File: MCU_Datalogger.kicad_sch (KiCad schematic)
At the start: 25 parts, among them U1 24LC1025, U2 24LC1025, U3 DS1337S_, U4 ATMEGA328P-AUR, Y1 Crystal, Y2 Crystal

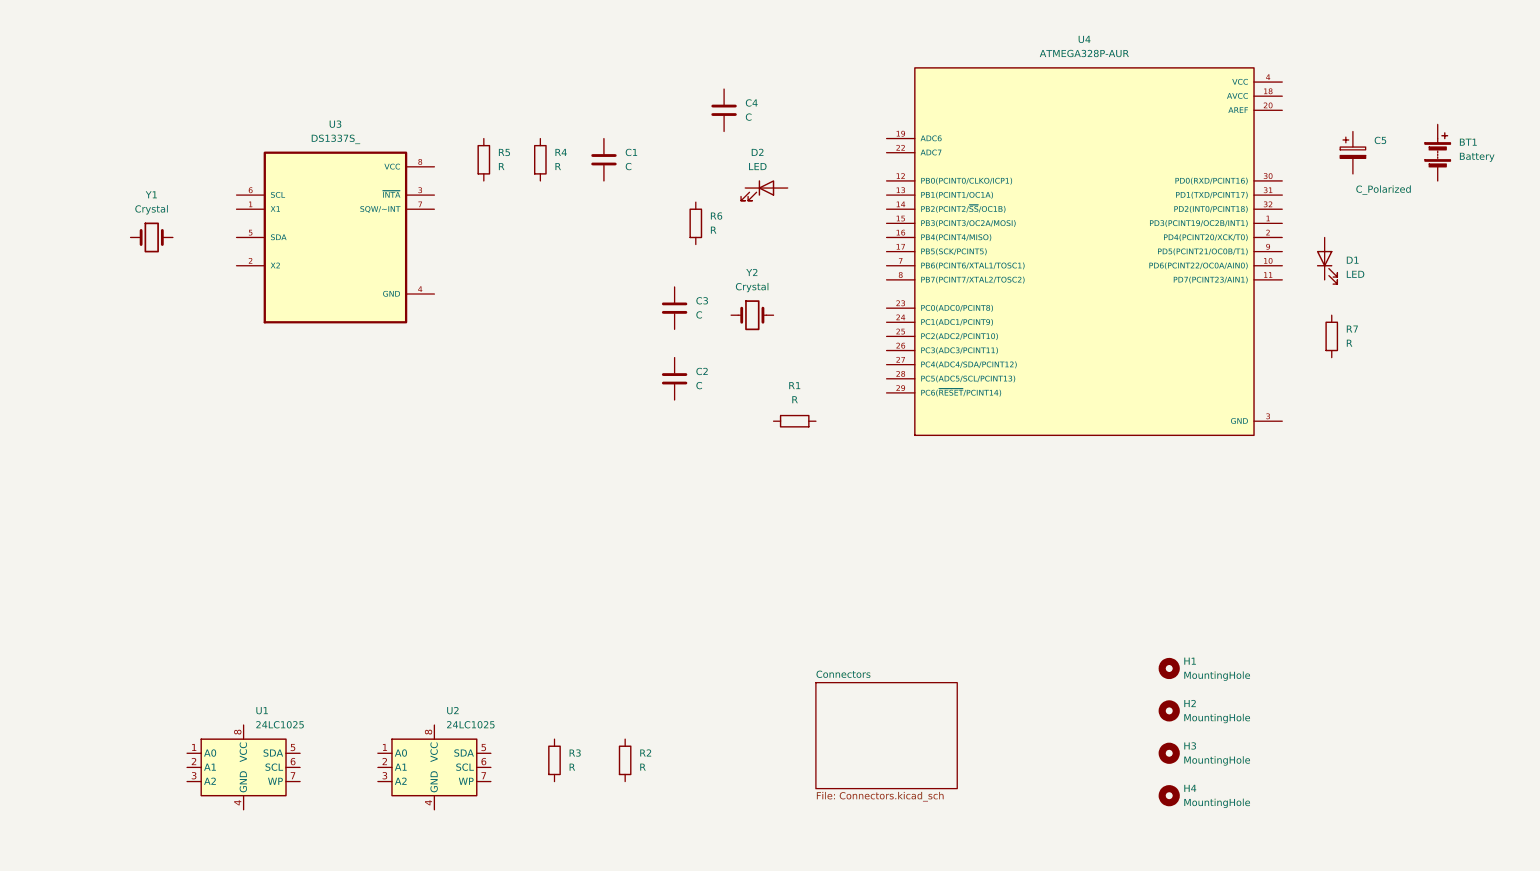
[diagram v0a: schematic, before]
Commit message: Added componant values
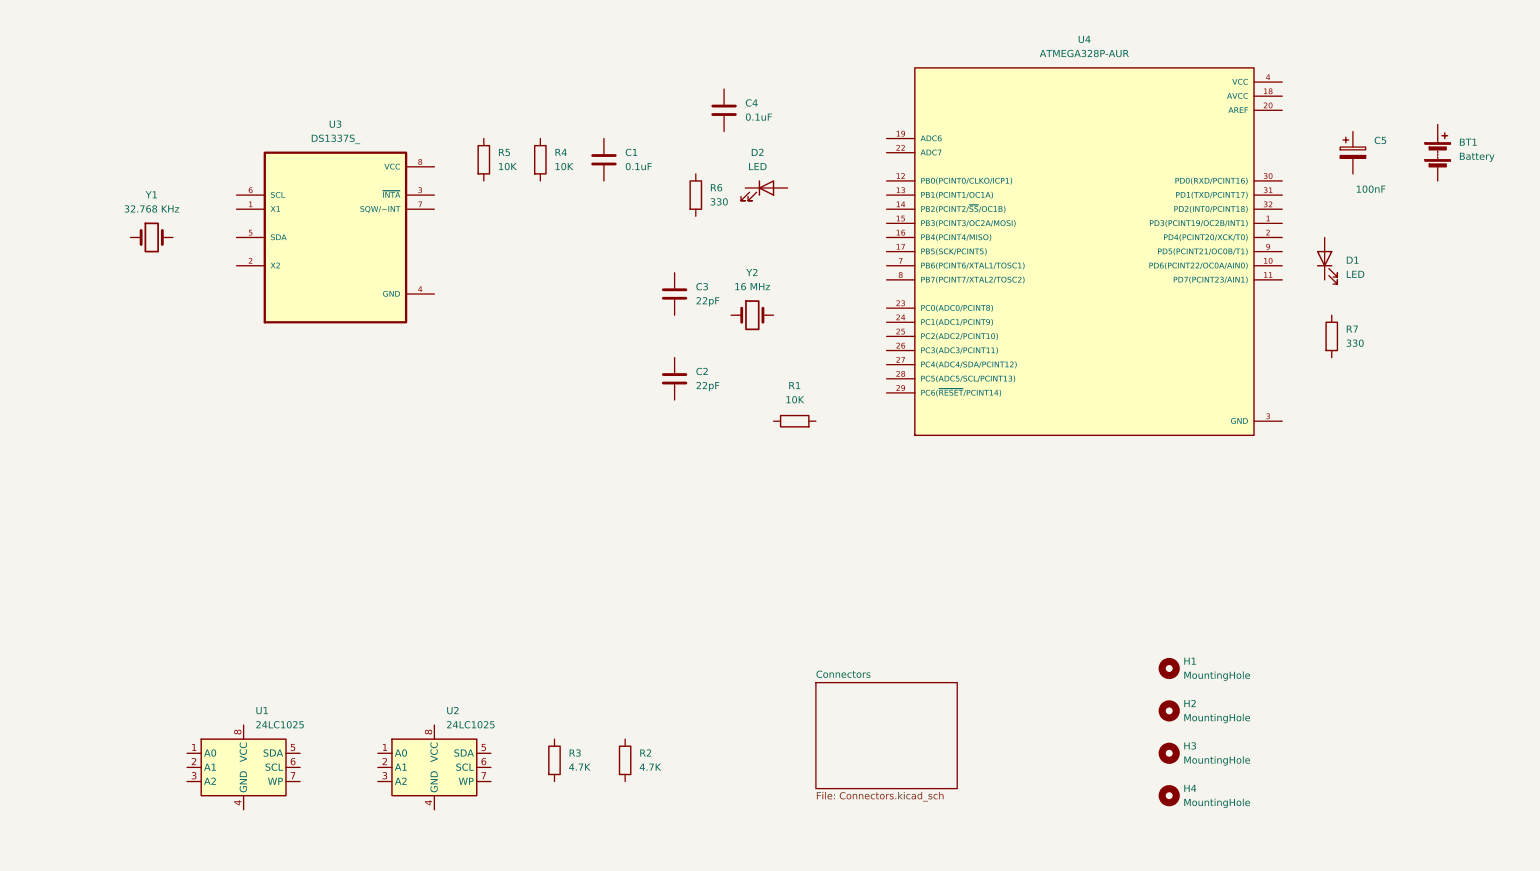
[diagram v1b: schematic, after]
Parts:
- C1, C4: value C -> 0.1uF
- C2, C3: value C -> 22pF
- C5: value C_Polarized -> 100nF
- R1: value R -> 10K; Purpose (none) -> Pull-Up resistor
- R2, R3: value R -> 4.7K
- R4, R5: value R -> 10K
- R6, R7: value R -> 330
- Y1: value Crystal -> 32.768 KHz
- Y2: value Crystal -> 16 MHz
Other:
- moved on the sheet: C3, R6
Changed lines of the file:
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@@
 			)
 		)
-		(property "Value" "C"
+		(property "Value" "0.1uF"
 			(at 146.05 38.0999 0)
 			(effects
@@
 			)
 		)
-		(property "Value" "C"
+		(property "Value" "0.1uF"
 			(at 124.46 46.9899 0)
 			(effects
@@
 			)
 		)
-		(property "Value" "C_Polarized"
+		(property "Value" "100nF"
 			(at 255.778 51.054 0)
 			(effects
@@
 			)
 		)
-		(property "Value" "C"
+		(property "Value" "22pF"
 			(at 137.16 86.3599 0)
 			(effects
@@
 			)
 		)
-		(property "Value" "R"
+		(property "Value" "4.7K"
 			(at 114.3 154.9399 0)
 			(effects
@@
 			)
 		)
-		(property "Value" "R"
+		(property "Value" "10K"
 			(at 111.76 46.9899 0)
 			(effects
@@
 			)
 		)
-		(property "Value" "R"
+		(property "Value" "330"
 			(at 254 78.7399 0)
 			(effects
@@
 	(symbol
 		(lib_id "Device:C")
-		(at 133.35 72.39 0)
+		(at 133.35 69.85 0)
 		(unit 1)
 		(exclude_from_sim no)
@@
 		(fields_autoplaced yes)
 		(property "Reference" "C3"
+			(at 137.16 68.5799 0)
+			(effects
+				(font
+					(size 1.27 1.27)
+				)
+				(justify left)
+			)
+		)
+		(property "Value" "22pF"
 			(at 137.16 71.1199 0)
 			(effects
@@
 			)
 		)
-		(property "Value" "C"
-			(at 137.16 73.6599 0)
-			(effects
-				(font
-					(size 1.27 1.27)
-				)
-				(justify left)
-			)
-		)
-		(property "Footprint" ""
-			(at 134.3152 76.2 0)
+		(property "Footprint" ""
+			(at 134.3152 73.66 0)
 			(effects
 				(font
@@
 		)
 		(property "Datasheet" "~"
-			(at 133.35 72.39 0)
+			(at 133.35 69.85 0)
 			(effects
 				(font
@@
 		)
 		(property "Description" "Unpolarized capacitor"
-			(at 133.35 72.39 0)
+			(at 133.35 69.85 0)
 			(effects
 				(font
@@
 			)
 		)
-		(property "Value" "R"
+		(property "Value" "10K"
 			(at 101.6 46.9899 0)
 			(effects
@@
 			)
 		)
-		(property "Value" "R"
+		(property "Value" "4.7K"
 			(at 127 154.9399 0)
 			(effects
@@
 			)
 		)
-		(property "Value" "Crystal"
+		(property "Value" "32.768 KHz"
 			(at 39.37 54.61 0)
 			(effects
@@
 	(symbol
 		(lib_id "Device:R")
-		(at 137.16 57.15 0)
+		(at 137.16 52.07 0)
 		(unit 1)
 		(exclude_from_sim no)
@@
 		(fields_autoplaced yes)
 		(property "Reference" "R6"
-			(at 139.7 55.8799 0)
-			(effects
-				(font
-					(size 1.27 1.27)
-				)
-				(justify left)
-			)
-		)
-		(property "Value" "R"
-			(at 139.7 58.4199 0)
-			(effects
-				(font
-					(size 1.27 1.27)
-				)
-				(justify left)
-			)
-		)
-		(property "Footprint" ""
-			(at 135.382 57.15 90)
+			(at 139.7 50.7999 0)
+			(effects
+				(font
+					(size 1.27 1.27)
+				)
+				(justify left)
+			)
+		)
+		(property "Value" "330"
+			(at 139.7 53.3399 0)
+			(effects
+				(font
+					(size 1.27 1.27)
+				)
+				(justify left)
+			)
+		)
+		(property "Footprint" ""
+			(at 135.382 52.07 90)
 			(effects
 				(font
@@
 		)
 		(property "Datasheet" "~"
-			(at 137.16 57.15 0)
+			(at 137.16 52.07 0)
 			(effects
 				(font
@@
 		)
 		(property "Description" "Resistor"
-			(at 137.16 57.15 0)
+			(at 137.16 52.07 0)
 			(effects
 				(font
@@
 			)
 		)
-		(property "Value" "R"
+		(property "Value" "10K"
 			(at 154.94 88.9 90)
 			(effects
@@
 			)
 		)
+		(property "Purpose" "Pull-Up resistor"
+			(at 154.94 92.71 90)
+			(effects
+				(font
+					(size 1.27 1.27)
+				)
+				(hide yes)
+			)
+		)
 		(pin "1"
 		)
@@
 			)
 		)
-		(property "Value" "Crystal"
+		(property "Value" "16 MHz"
 			(at 147.32 68.58 0)
 			(effects

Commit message: Associated footprints to Symbols
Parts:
- BT1: footprint (none) -> Connector_PinHeader_2.54mm:PinHeader_1x02_P2.54mm_Vertical
- C1, C2, C3, C4, C5: footprint (none) -> Capacitor_SMD:C_0805_2012Metric
- D1, D2: footprint (none) -> LED_SMD:LED_0805_2012Metric
- H1, H2, H3, H4: footprint (none) -> MountingHole:MountingHole_2.1mm
- R1, R2, R3, R4, R5, R6, R7: footprint (none) -> Resistor_SMD:R_0805_2012Metric
- U1, U2: footprint (none) -> Package_SO:SOIC-8_5.3x5.3mm_P1.27mm
- U3: footprint DS1337S_:SOIC127P600X175-8N -> Footprints:SOIC127P600X175-8N
- U4: footprint ATMEGA328P-AUR:QFP80P900X900X120-32N -> Footprints:QFP80P900X900X120-32N
- Y1, Y2: footprint (none) -> Crystal:Crystal_SMD_5032-2Pin_5.0x3.2mm_HandSoldering
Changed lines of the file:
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@@
 			)
 		)
-		(property "Footprint" ""
+		(property "Footprint" "Connector_PinHeader_2.54mm:PinHeader_1x02_P2.54mm_Vertical"
 			(at 270.51 42.926 90)
 			(effects
@@
 			)
 		)
-		(property "Footprint" ""
+		(property "Footprint" "Capacitor_SMD:C_0805_2012Metric"
 			(at 143.2052 40.64 0)
 			(effects
@@
 			)
 		)
-		(property "Footprint" ""
+		(property "Footprint" "Capacitor_SMD:C_0805_2012Metric"
 			(at 121.6152 49.53 0)
 			(effects
@@
 			)
 		)
-		(property "Footprint" ""
+		(property "Footprint" "Capacitor_SMD:C_0805_2012Metric"
 			(at 256.2352 48.26 0)
 			(effects
@@
 			)
 		)
-		(property "Footprint" ""
+		(property "Footprint" "MountingHole:MountingHole_2.1mm"
 			(at 222.25 160.02 0)
 			(effects
@@
 			)
 		)
-		(property "Footprint" "DS1337S_:SOIC127P600X175-8N"
+		(property "Footprint" "Footprints:SOIC127P600X175-8N"
 			(at 72.39 59.69 0)
 			(effects
@@
 			)
 		)
-		(property "Footprint" ""
+		(property "Footprint" "Capacitor_SMD:C_0805_2012Metric"
 			(at 134.3152 88.9 0)
 			(effects
@@
 			)
 		)
-		(property "Footprint" ""
+		(property "Footprint" "Resistor_SMD:R_0805_2012Metric"
 			(at 109.982 153.67 90)
 			(effects
@@
 			)
 		)
-		(property "Footprint" ""
+		(property "Footprint" "Resistor_SMD:R_0805_2012Metric"
 			(at 107.442 45.72 90)
 			(effects
@@
 			)
 		)
-		(property "Footprint" ""
+		(property "Footprint" "Resistor_SMD:R_0805_2012Metric"
 			(at 249.682 77.47 90)
 			(effects
@@
 			)
 		)
-		(property "Footprint" ""
+		(property "Footprint" "Capacitor_SMD:C_0805_2012Metric"
 			(at 134.3152 73.66 0)
 			(effects
@@
 			)
 		)
-		(property "Footprint" ""
+		(property "Footprint" "Resistor_SMD:R_0805_2012Metric"
 			(at 97.282 45.72 90)
 			(effects
@@
 			)
 		)
-		(property "Footprint" ""
+		(property "Footprint" "MountingHole:MountingHole_2.1mm"
 			(at 222.25 152.4 0)
 			(effects
@@
 			)
 		)
-		(property "Footprint" ""
+		(property "Footprint" "MountingHole:MountingHole_2.1mm"
 			(at 222.25 144.78 0)
 			(effects
@@
 			)
 		)
-		(property "Footprint" ""
+		(property "Footprint" "Package_SO:SOIC-8_5.3x5.3mm_P1.27mm"
 			(at 55.88 154.94 0)
 			(effects
@@
 			)
 		)
-		(property "Footprint" ""
+		(property "Footprint" "Resistor_SMD:R_0805_2012Metric"
 			(at 122.682 153.67 90)
 			(effects
@@
 			)
 		)
-		(property "Footprint" "ATMEGA328P-AUR:QFP80P900X900X120-32N"
+		(property "Footprint" "Footprints:QFP80P900X900X120-32N"
 			(at 207.01 62.23 0)
 			(effects
@@
 			)
 		)
-		(property "Footprint" ""
+		(property "Footprint" "Crystal:Crystal_SMD_5032-2Pin_5.0x3.2mm_HandSoldering"
 			(at 39.37 59.69 0)
 			(effects
@@
 			)
 		)
-		(property "Footprint" ""
+		(property "Footprint" "Resistor_SMD:R_0805_2012Metric"
 			(at 135.382 52.07 90)
 			(effects
@@
 			)
 		)
-		(property "Footprint" ""
+		(property "Footprint" "Resistor_SMD:R_0805_2012Metric"
 			(at 154.94 94.488 90)
 			(effects
@@
 			)
 		)
-		(property "Footprint" ""
+		(property "Footprint" "LED_SMD:LED_0805_2012Metric"
 			(at 149.86 50.8 0)
 			(effects
@@
 			)
 		)
-		(property "Footprint" ""
+		(property "Footprint" "Crystal:Crystal_SMD_5032-2Pin_5.0x3.2mm_HandSoldering"
 			(at 147.32 73.66 0)
 			(effects
@@
 			)
 		)
-		(property "Footprint" ""
+		(property "Footprint" "Package_SO:SOIC-8_5.3x5.3mm_P1.27mm"
 			(at 90.17 154.94 0)
 			(effects
@@
 			)
 		)
-		(property "Footprint" ""
+		(property "Footprint" "LED_SMD:LED_0805_2012Metric"
 			(at 250.19 63.5 0)
 			(effects
@@
 			)
 		)
-		(property "Footprint" ""
+		(property "Footprint" "MountingHole:MountingHole_2.1mm"
 			(at 222.25 137.16 0)
 			(effects

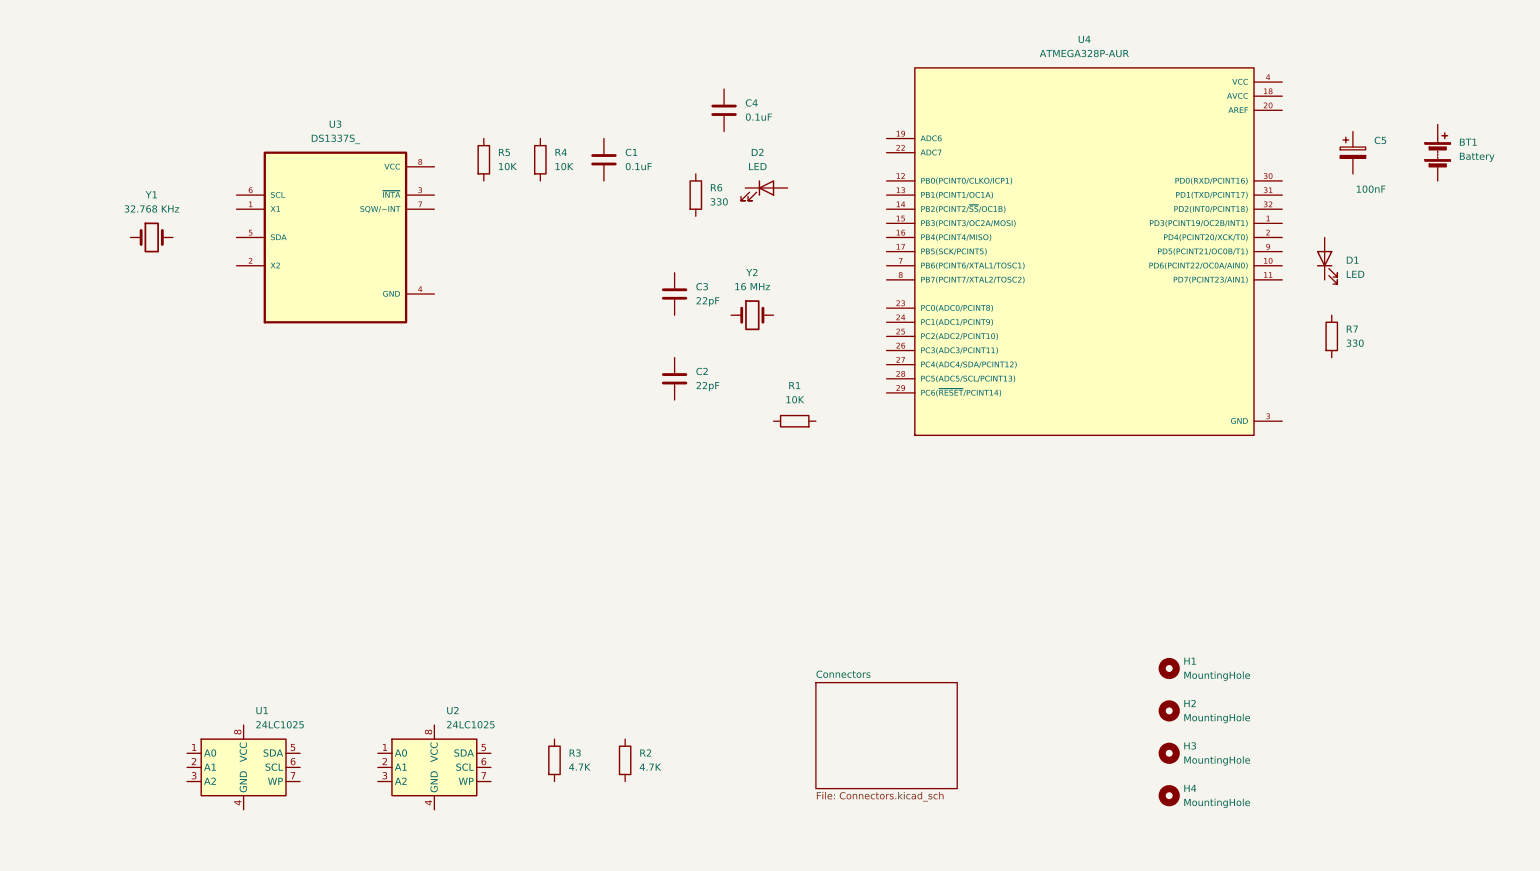
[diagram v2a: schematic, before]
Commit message: Completed Wiring of the main sheet
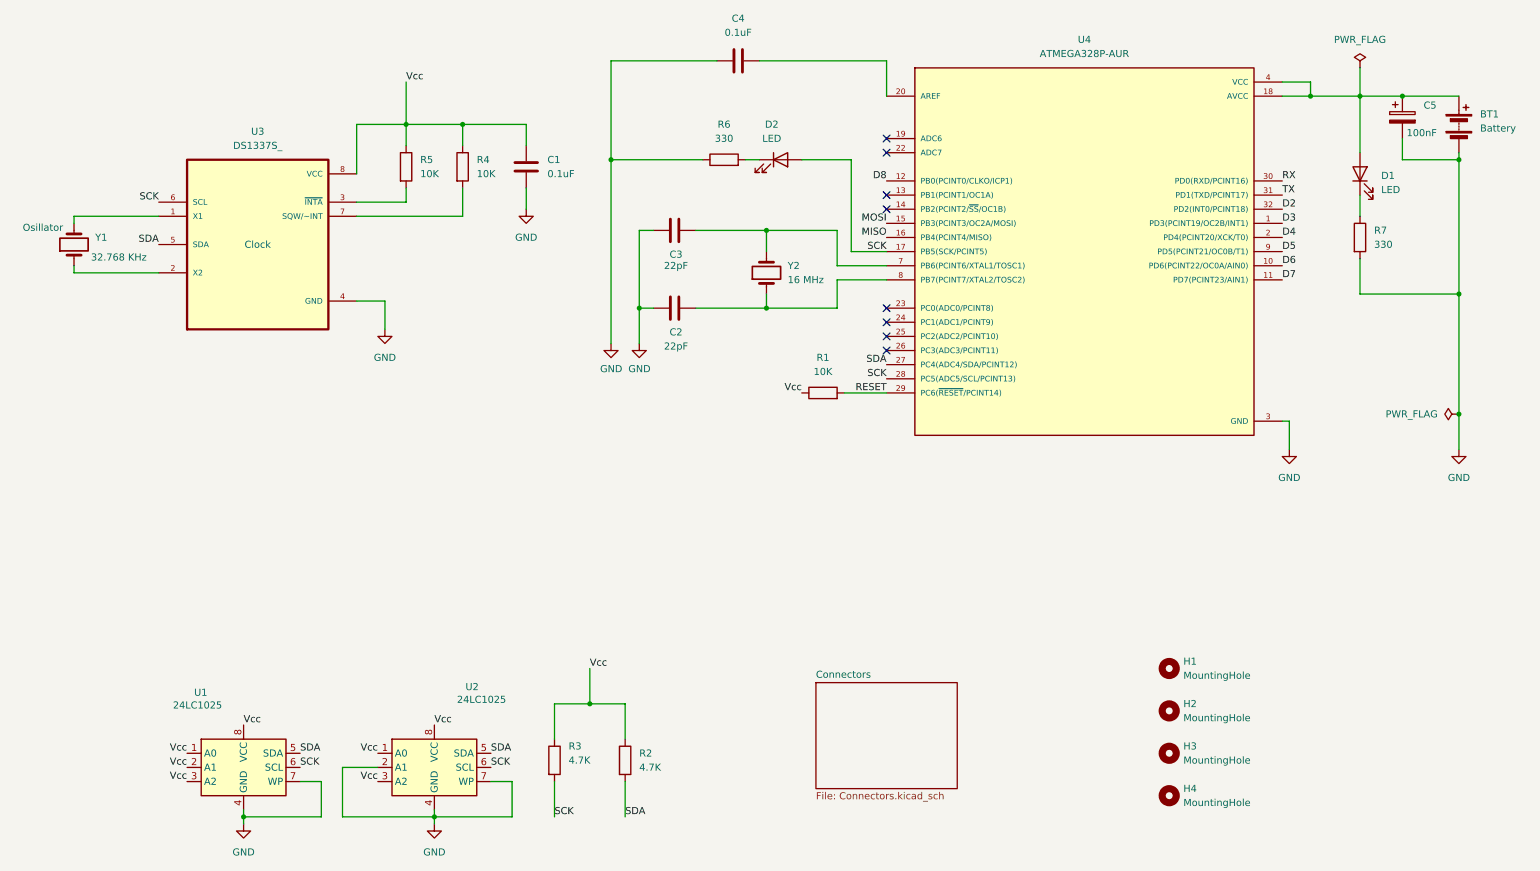
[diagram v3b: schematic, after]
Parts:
- R2, R3: Purpose (none) -> Pull Up Resisitor
- U3: Purpose (none) -> Clock
- Y1: Purpose (none) -> Osillator
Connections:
- net GND: now also BT1.2 (-), C1.2, C2.1, C3.1, C4.1, C5.2, R6.1, R7.2, U1.4 (GND), U1.7 (WP), U2.2 (A1), U2.4 (GND), U2.7 (WP), U3.4 (GND)
- net VCC: now also BT1.1 (+), C5.1, D1.2 (A), U4.18 (AVCC)
- net at C4.2: now also U4.20 (AREF)
- net Vcc: now reaches C1.1
- net Vcc: now also R1.1, R2.1, R3.1, R4.1, R5.1, U1.1 (A0), U1.2 (A1), U1.3 (A2), U1.8 (VCC), U2.1 (A0), U2.3 (A2), U2.8 (VCC), U3.8 (VCC)
- net at U3.1 (X1): now also Y1.2
- net at U3.2 (X2): now also Y1.1
- net at U3.3 (~{INTA}): now also R5.2
- net SDA: now reaches U3.5 (SDA)
- net SDA: now also R2.2, U1.5 (SDA), U2.5 (SDA), U4.27 (PC4(ADC4/SDA/PCINT12))
- net SCK: now reaches U3.6 (SCL)
- net SCK: now also D2.2 (A), R3.2, U1.6 (SCL), U2.6 (SCL), U4.17 (PB5(SCK/PCINT5)), U4.28 (PC5(ADC5/SCL/PCINT13))
- net at U3.7 (SQW/~INT): now also R4.2
- net at C2.2: now also U4.8 (PB7(PCINT7/XTAL2/TOSC2)), Y2.1
- net at R7.1: now also D1.1 (K)
- net at C3.2: now also U4.7 (PB6(PCINT6/XTAL1/TOSC1)), Y2.2
- net D3: now reaches U4.1 (PD3(PCINT19/OC2B/INT1))
- net D6: now reaches U4.10 (PD6(PCINT22/OC0A/AIN0))
- net D7: now reaches U4.11 (PD7(PCINT23/AIN1))
- net D8: now reaches U4.12 (PB0(PCINT0/CLKO/ICP1))
- net MOSI: now reaches U4.15 (PB3(PCINT3/OC2A/MOSI))
- net MISO: now reaches U4.16 (PB4(PCINT4/MISO))
- net D4: now reaches U4.2 (PD4(PCINT20/XCK/T0))
- net RESET: now reaches U4.29 (PC6(~{RESET}/PCINT14))
- net RESET: now also R1.2
- net RX: now reaches U4.30 (PD0(RXD/PCINT16))
- net TX: now reaches U4.31 (PD1(TXD/PCINT17))
- net D2: now reaches U4.32 (PD2(INT0/PCINT18))
- net D5: now reaches U4.9 (PD5(PCINT21/OC0B/T1))
- net at R6.2: now also D2.1 (K)
- no-connect marks 0 -> 8
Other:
- moved on the sheet: BT1, C1, C2, C3, C4, C5, D1, D2, R1, R4, R5, R6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

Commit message: Completed wiring on second sheet and introduced hierarchial nets
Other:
- sheet Connectors ports: added D2, D3, D4, D5, D6, D7, D8, GND, MISO, MOSI, RESET, RX, SCK, SDA, TX, Vcc; removed none
- moved on the sheet: H1, H2, H3, H4
